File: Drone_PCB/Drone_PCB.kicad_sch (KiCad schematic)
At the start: 56 parts, among them J1 Conn_01x04_Pin, J2 Conn_01x08_Socket, J3 Conn_01x05_Socket, J4 Conn_01x02_Socket, J5 Conn_01x02_Socket, J6 Conn_01x02_Socket, J6 USB_B_Micro, J7 Conn_01x02_Socket, J8 Conn_01x02_Socket, Q1 BSS214NW, Q2 BSS214NW, Q3 AO3400A, Q4 AO3400A, Q5 AO3400A, Q6 AO3400A, SW2 SW_DPST_x2, U1 STM32F411RCT6, U2 AP2112K-3.3, U3 TP4056-42-ESOP8, U4 DW01A, Y1 26MHz

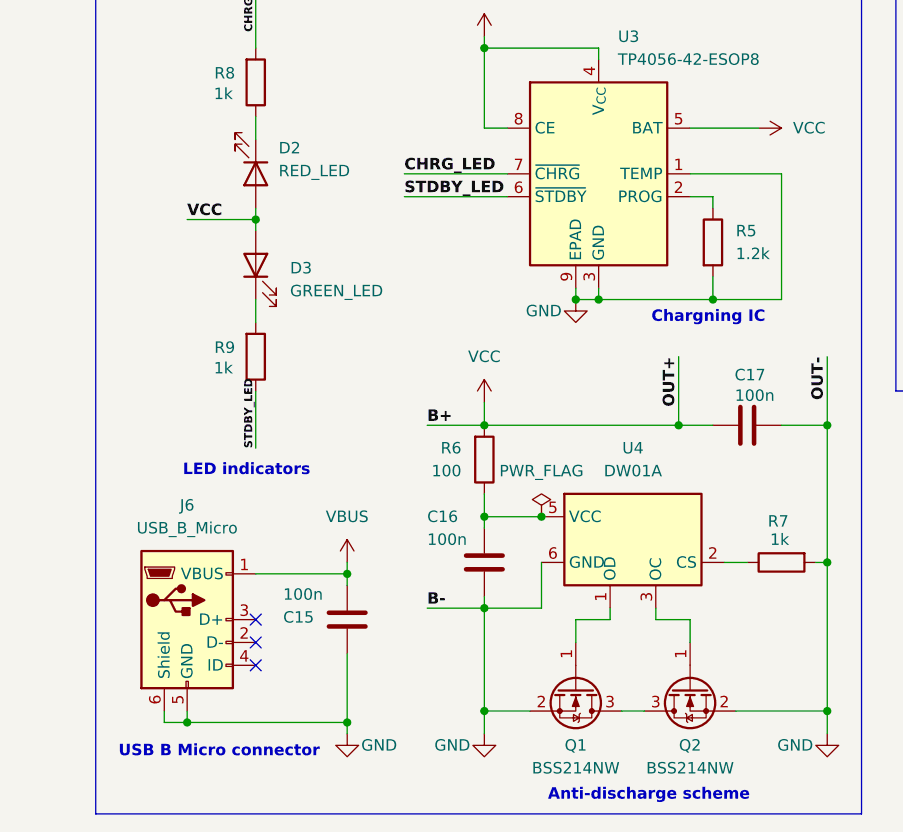
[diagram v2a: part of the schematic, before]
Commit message: Updated charging section
Changed NMOS transistors + diodes to VBUS
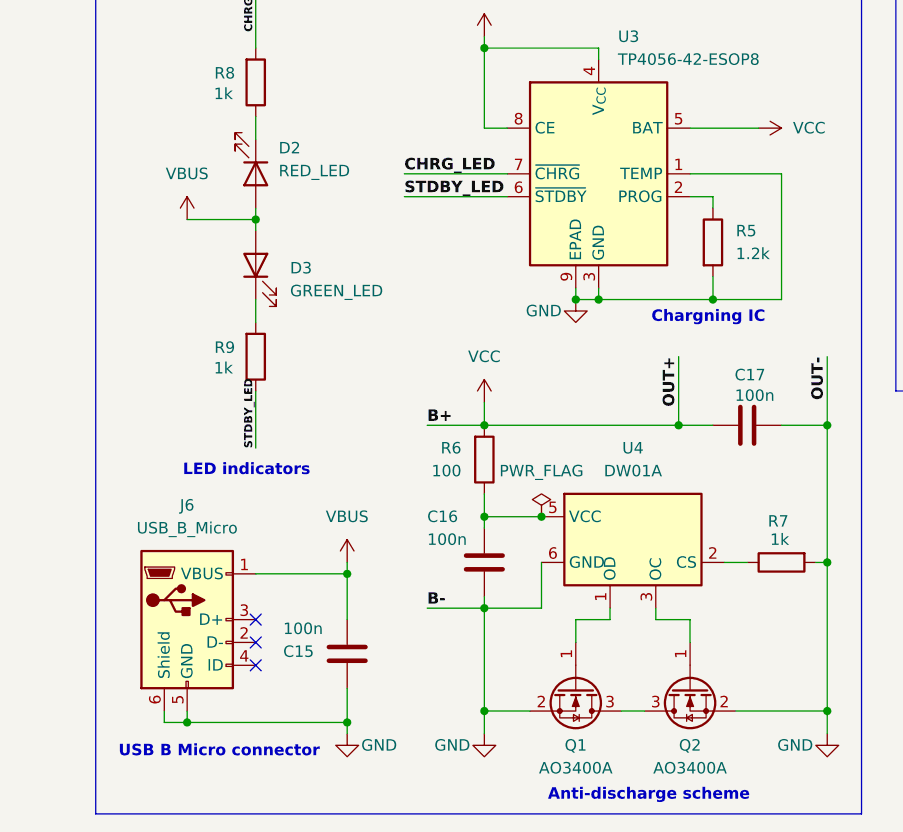
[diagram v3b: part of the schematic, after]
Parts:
- removed Q1, Q2: BSS214NW, Package_TO_SOT_SMD:SOT-323_SC-70, symbol Transistor_FET:BSS214NW
- added Q1, Q2: AO3400A, Package_TO_SOT_SMD:SOT-23, symbol Transistor_FET:AO3400A
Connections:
- net +3.3V: no longer D2.2 (A), D3.2 (A)
- net GND: now also Q1.2 (S), Q2.2 (S)
- net VBUS: now also D2.2 (A), D3.2 (A)
- net at U4.1 (OD): now also Q1.1 (G)
- net at U4.3 (OC): now also Q2.1 (G)
- new net: Q1.3 (D), Q2.3 (D)
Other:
- moved on the sheet: C15
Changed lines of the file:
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@@
 	)
 	(junction
+		(at 45.72 185.42)
+		(diameter 0)
+		(color 0 0 0 0)
+	)
+	(junction
 		(at 231.14 54.61)
 		(diameter 0)
@@
 	)
 	(junction
-		(at 45.72 185.42)
-		(diameter 0)
-		(color 0 0 0 0)
-	)
-	(junction
 		(at 220.98 132.08)
 		(diameter 0)
@@
 	(wire
 		(pts
+			(xy 45.72 181.61) (xy 45.72 185.42)
+		)
+		(stroke
+			(width 0)
+			(type default)
+		)
+	)
+	(wire
+		(pts
 			(xy 124.46 41.91) (xy 124.46 40.64)
 		)
@@
 	(wire
 		(pts
-			(xy 45.72 177.8) (xy 45.72 185.42)
-		)
-		(stroke
-			(width 0)
-			(type default)
-		)
-	)
-	(wire
-		(pts
 			(xy 43.18 45.72) (xy 48.26 45.72)
 		)
@@
 	(wire
 		(pts
-			(xy 45.72 168.91) (xy 45.72 170.18)
+			(xy 45.72 168.91) (xy 45.72 173.99)
 		)
 		(stroke
@@
 		)
 	)
-	(label "VCC"
-		(at 27.94 129.54 0)
-		(effects
-			(font
-				(size 1.27 1.27)
-				(thickness 0.254)
-				(bold yes)
-			)
-			(justify left bottom)
-		)
-	)
 	(label "UART_TX"
 		(at 156.21 88.9 0)
@@
 	)
 	(symbol
+		(lib_id "Transistor_FET:AO3400A")
+		(at 71.12 181.61 270)
+		(unit 1)
+		(exclude_from_sim no)
+		(in_bom yes)
+		(on_board yes)
+		(dnp no)
+		(fields_autoplaced yes)
+		(property "Reference" "Q1"
+			(at 71.12 187.96 90)
+			(effects
+				(font
+					(size 1.27 1.27)
+				)
+			)
+		)
+		(property "Value" "AO3400A"
+			(at 71.12 190.5 90)
+			(effects
+				(font
+					(size 1.27 1.27)
+				)
+			)
+		)
+		(property "Footprint" "Package_TO_SOT_SMD:SOT-23"
+			(at 69.215 186.69 0)
+			(effects
+				(font
+					(size 1.27 1.27)
+					(italic yes)
+				)
+				(justify left)
+				(hide yes)
+			)
+		)
+		(property "Datasheet" "http://www.aosmd.com/pdfs/datasheet/AO3400A.pdf"
+			(at 67.31 186.69 0)
+			(effects
+				(font
+					(size 1.27 1.27)
+				)
+				(justify left)
+				(hide yes)
+			)
+		)
+		(property "Description" "30V Vds, 5.7A Id, N-Channel MOSFET, SOT-23"
+			(at 71.12 181.61 0)
+			(effects
+				(font
+					(size 1.27 1.27)
+				)
+				(hide yes)
+			)
+		)
+		(pin "2"
+		)
+		(pin "3"
+		)
+		(pin "1"
+		)
+		(instances
+			(project "Drone_PCB"
+				(path "/2c198202-91eb-4035-8605-360d42f3c3f5"
+					(reference "Q1")
+					(unit 1)
+				)
+			)
+		)
+	)
+	(symbol
 		(lib_id "Switch:SW_DPST_x2")
 		(at 31.75 45.72 0)
@@
 	)
 	(symbol
-		(lib_id "Transistor_FET:BSS214NW")
-		(at 71.12 181.61 270)
-		(unit 1)
-		(exclude_from_sim no)
-		(in_bom yes)
-		(on_board yes)
-		(dnp no)
-		(fields_autoplaced yes)
-		(property "Reference" "Q1"
-			(at 71.12 187.96 90)
-			(effects
-				(font
-					(size 1.27 1.27)
-				)
-			)
-		)
-		(property "Value" "BSS214NW"
-			(at 71.12 190.5 90)
-			(effects
-				(font
-					(size 1.27 1.27)
-				)
-			)
-		)
-		(property "Footprint" "Package_TO_SOT_SMD:SOT-323_SC-70"
-			(at 69.215 186.69 0)
-			(effects
-				(font
-					(size 1.27 1.27)
-					(italic yes)
-				)
-				(justify left)
-				(hide yes)
-			)
-		)
-		(property "Datasheet" "https://www.infineon.com/dgdl/Infineon-BSS214NW-DS-v02_02-en.pdf?fileId=db3a30431b3e89eb011b695aebc01bde"
-			(at 67.31 186.69 0)
-			(effects
-				(font
-					(size 1.27 1.27)
-				)
-				(justify left)
-				(hide yes)
-			)
-		)
-		(property "Description" "20V Vds, 1.5A Id, N-Channel MOSFET, SOT-323"
-			(at 71.12 181.61 0)
-			(effects
-				(font
-					(size 1.27 1.27)
-				)
-				(hide yes)
-			)
-		)
-		(pin "1"
-		)
-		(pin "3"
-		)
-		(pin "2"
-		)
-		(instances
-			(project ""
-				(path "/2c198202-91eb-4035-8605-360d42f3c3f5"
-					(reference "Q1")
-					(unit 1)
-				)
-			)
-		)
-	)
-	(symbol
 		(lib_id "Device:R")
 		(at 93.98 167.64 90)
@@
 	(symbol
 		(lib_id "Device:C")
-		(at 45.72 173.99 0)
+		(at 45.72 177.8 0)
 		(mirror x)
 		(unit 1)
@@
 		(dnp no)
 		(property "Reference" "C15"
-			(at 38.608 173.736 0)
+			(at 38.608 177.546 0)
 			(effects
 				(font
@@
 		)
 		(property "Value" "100n"
-			(at 38.608 171.196 0)
+			(at 38.608 175.006 0)
 			(effects
 				(font
@@
 		)
 		(property "Footprint" "Capacitor_SMD:C_0402_1005Metric"
-			(at 46.6852 170.18 0)
+			(at 46.6852 173.99 0)
 			(effects
 				(font
@@
 		)
 		(property "Datasheet" "~"
-			(at 45.72 173.99 0)
+			(at 45.72 177.8 0)
 			(effects
 				(font
@@
 		)
 		(property "Description" "Unpolarized capacitor"
-			(at 45.72 173.99 0)
+			(at 45.72 177.8 0)
 			(effects
 				(font
@@
 	)
 	(symbol
+		(lib_id "power:VBUS")
+		(at 27.94 129.54 0)
+		(unit 1)
+		(exclude_from_sim no)
+		(in_bom yes)
+		(on_board yes)
+		(dnp no)
+		(fields_autoplaced yes)
+		(property "Reference" "#PWR033"
+			(at 27.94 133.35 0)
+			(effects
+				(font
+					(size 1.27 1.27)
+				)
+				(hide yes)
+			)
+		)
+		(property "Value" "VBUS"
+			(at 27.94 124.46 0)
+			(effects
+				(font
+					(size 1.27 1.27)
+				)
+			)
+		)
+		(property "Footprint" ""
+			(at 27.94 129.54 0)
+			(effects
+				(font
+					(size 1.27 1.27)
+				)
+				(hide yes)
+			)
+		)
+		(property "Datasheet" ""
+			(at 27.94 129.54 0)
+			(effects
+				(font
+					(size 1.27 1.27)
+				)
+				(hide yes)
+			)
+		)
+		(property "Description" "Power symbol creates a global label with name \"VBUS\""
+			(at 27.94 129.54 0)
+			(effects
+				(font
+					(size 1.27 1.27)
+				)
+				(hide yes)
+			)
+		)
+		(pin "1"
+		)
+		(instances
+			(project "Drone_PCB"
+				(path "/2c198202-91eb-4035-8605-360d42f3c3f5"
+					(reference "#PWR033")
+					(unit 1)
+				)
+			)
+		)
+	)
+	(symbol
 		(lib_id "Battery_Management:DW01A")
 		(at 77.47 165.1 0)
@@
 	)
 	(symbol
+		(lib_id "Transistor_FET:AO3400A")
+		(at 83.82 181.61 90)
+		(mirror x)
+		(unit 1)
+		(exclude_from_sim no)
+		(in_bom yes)
+		(on_board yes)
+		(dnp no)
+		(property "Reference" "Q2"
+			(at 83.82 187.96 90)
+			(effects
+				(font
+					(size 1.27 1.27)
+				)
+			)
+		)
+		(property "Value" "AO3400A"
+			(at 83.82 190.5 90)
+			(effects
+				(font
+					(size 1.27 1.27)
+				)
+			)
+		)
+		(property "Footprint" "Package_TO_SOT_SMD:SOT-23"
+			(at 85.725 186.69 0)
+			(effects
+				(font
+					(size 1.27 1.27)
+					(italic yes)
+				)
+				(justify left)
+				(hide yes)
+			)
+		)
+		(property "Datasheet" "http://www.aosmd.com/pdfs/datasheet/AO3400A.pdf"
+			(at 87.63 186.69 0)
+			(effects
+				(font
+					(size 1.27 1.27)
+				)
+				(justify left)
+				(hide yes)
+			)
+		)
+		(property "Description" "30V Vds, 5.7A Id, N-Channel MOSFET, SOT-23"
+			(at 83.82 181.61 0)
+			(effects
+				(font
+					(size 1.27 1.27)
+				)
+				(hide yes)
+			)
+		)
+		(pin "2"
+		)
+		(pin "3"
+		)
+		(pin "1"
+		)
+		(instances
+			(project "Drone_PCB"
+				(path "/2c198202-91eb-4035-8605-360d42f3c3f5"
+					(reference "Q2")
+					(unit 1)
+				)
+			)
+		)
+	)
+	(symbol
 		(lib_id "power:+3.3V")
 		(at 228.6 142.24 180)
@@
 					(unit 1)
 				)
-			)
-		)
-	)
-	(symbol
-		(lib_id "Transistor_FET:BSS214NW")
-		(at 83.82 181.61 90)
-		(mirror x)
-		(unit 1)
-		(exclude_from_sim no)
-		(in_bom yes)
-		(on_board yes)
-		(dnp no)
-		(property "Reference" "Q2"
-			(at 83.82 187.96 90)
-			(effects
-				(font
-					(size 1.27 1.27)
-				)
-			)
-		)
-		(property "Value" "BSS214NW"
-			(at 83.82 190.5 90)
-			(effects
-				(font
-					(size 1.27 1.27)
-				)
-			)
-		)
-		(property "Footprint" "Package_TO_SOT_SMD:SOT-323_SC-70"
-			(at 85.725 186.69 0)
-			(effects
-				(font
-					(size 1.27 1.27)
-					(italic yes)
-				)
-				(justify left)
-				(hide yes)
-			)
-		)
-		(property "Datasheet" "https://www.infineon.com/dgdl/Infineon-BSS214NW-DS-v02_02-en.pdf?fileId=db3a30431b3e89eb011b695aebc01bde"
-			(at 87.63 186.69 0)
-			(effects
-				(font
-					(size 1.27 1.27)
-				)
-				(justify left)
-				(hide yes)
-			)
-		)
-		(property "Description" "20V Vds, 1.5A Id, N-Channel MOSFET, SOT-323"
-			(at 83.82 181.61 0)
-			(effects
-				(font
-					(size 1.27 1.27)
-				)
-				(hide yes)
-			)
-		)
-		(pin "1"
-		)
-		(pin "3"
-		)
-		(pin "2"
-		)
-		(instances
-			(project "Drone_PCB"
-				(path "/2c198202-91eb-4035-8605-360d42f3c3f5"
-					(reference "Q2")
-					(unit 1)
-				)

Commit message: Added NRST button
Following the advice of Dr. Puchalski, I added NRST button. Additionally, I tidied up the engine area more.
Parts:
- added SW1: SW_MEC_5G, symbol Switch:SW_MEC_5G
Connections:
- net GND: now also SW1.3 (B), SW1.4 (B)
- net NRST: now also SW1.1 (A), SW1.2 (A)
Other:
- moved on the sheet: D6, D7, J1, J4, J5, J6, J7, Q5, Q6

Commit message: Switching THD Signal LED to SMD
It will be better I guess
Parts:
- removed J8: Conn_01x02_Socket, symbol Connector:Conn_01x02_Socket
- added D8: YELLOW_LED, symbol Device:LED
- added R11: 220, Resistor_SMD:R_0402_1005Metric, symbol Device:R
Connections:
- net GND: now also D8.1 (K)
- net LED_SIGNAL: now also R11.2
- new net: D8.2 (A), R11.1
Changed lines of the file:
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@@
 	(wire
 		(pts
-			(xy 148.59 105.41) (xy 154.94 105.41)
-		)
-		(stroke
-			(width 0)
-			(type default)
-		)
-	)
-	(wire
-		(pts
 			(xy 232.41 40.64) (xy 232.41 43.18)
 		)
@@
 	(wire
 		(pts
-			(xy 154.94 107.95) (xy 148.59 107.95)
-		)
-		(stroke
-			(width 0)
-			(type default)
-		)
-	)
-	(wire
-		(pts
 			(xy 147.32 40.64) (xy 147.32 41.91)
 		)
@@
 	(wire
 		(pts
+			(xy 154.94 107.95) (xy 154.94 109.22)
+		)
+		(stroke
+			(width 0)
+			(type default)
+		)
+	)
+	(wire
+		(pts
 			(xy 49.53 48.26) (xy 48.26 48.26)
 		)
@@
 	(wire
 		(pts
-			(xy 154.94 96.52) (xy 154.94 105.41)
-		)
-		(stroke
-			(width 0)
-			(type default)
-		)
-	)
-	(wire
-		(pts
 			(xy 35.56 138.43) (xy 35.56 140.97)
 		)
@@
 	(wire
 		(pts
-			(xy 154.94 109.22) (xy 154.94 107.95)
-		)
-		(stroke
-			(width 0)
-			(type default)
-		)
-	)
-	(wire
-		(pts
 			(xy 158.75 40.64) (xy 158.75 41.91)
 		)
@@
 	(wire
 		(pts
+			(xy 154.94 96.52) (xy 154.94 100.33)
+		)
+		(stroke
+			(width 0)
+			(type default)
+		)
+	)
+	(wire
+		(pts
 			(xy 228.6 104.14) (xy 228.6 105.41)
 		)
@@
 	)
 	(symbol
+		(lib_id "Device:LED")
+		(at 154.94 113.03 90)
+		(unit 1)
+		(exclude_from_sim no)
+		(in_bom yes)
+		(on_board yes)
+		(dnp no)
+		(property "Reference" "D8"
+			(at 146.05 112.776 90)
+			(effects
+				(font
+					(size 1.27 1.27)
+				)
+				(justify right)
+			)
+		)
+		(property "Value" "YELLOW_LED"
+			(at 141.986 115.316 90)
+			(effects
+				(font
+					(size 1.27 1.27)
+				)
+				(justify right)
+			)
+		)
+		(property "Footprint" ""
+			(at 154.94 113.03 0)
+			(effects
+				(font
+					(size 1.27 1.27)
+				)
+				(hide yes)
+			)
+		)
+		(property "Datasheet" "~"
+			(at 154.94 113.03 0)
+			(effects
+				(font
+					(size 1.27 1.27)
+				)
+				(hide yes)
+			)
+		)
+		(property "Description" "Light emitting diode"
+			(at 154.94 113.03 0)
+			(effects
+				(font
+					(size 1.27 1.27)
+				)
+				(hide yes)
+			)
+		)
+		(property "Sim.Pins" "1=K 2=A"
+			(at 154.94 113.03 0)
+			(effects
+				(font
+					(size 1.27 1.27)
+				)
+				(hide yes)
+			)
+		)
+		(pin "2"
+		)
+		(pin "1"
+		)
+		(instances
+			(project ""
+				(path "/2c198202-91eb-4035-8605-360d42f3c3f5"
+					(reference "D8")
+					(unit 1)
+				)
+			)
+		)
+	)
+	(symbol
 		(lib_id "Device:C")
 		(at 113.03 36.83 0)
@@
 	)
 	(symbol
-		(lib_id "Connector:Conn_01x02_Socket")
-		(at 143.51 107.95 180)
-		(unit 1)
-		(exclude_from_sim no)
-		(in_bom yes)
-		(on_board yes)
-		(dnp no)
-		(property "Reference" "J8"
-			(at 140.208 107.696 0)
-			(effects
-				(font
-					(size 1.27 1.27)
-				)
-			)
-		)
-		(property "Value" "Conn_01x02_Socket"
-			(at 140.208 110.236 0)
-			(effects
-				(font
-					(size 1.27 1.27)
-				)
-			)
-		)
-		(property "Footprint" ""
-			(at 143.51 107.95 0)
-			(effects
-				(font
-					(size 1.27 1.27)
-				)
-				(hide yes)
-			)
-		)
-		(property "Datasheet" "~"
-			(at 143.51 107.95 0)
-			(effects
-				(font
-					(size 1.27 1.27)
-				)
-				(hide yes)
-			)
-		)
-		(property "Description" "Generic connector, single row, 01x02, script generated"
-			(at 143.51 107.95 0)
-			(effects
-				(font
-					(size 1.27 1.27)
-				)
-				(hide yes)
-			)
-		)
-		(pin "1"
-		)
-		(pin "2"
-		)
-		(instances
-			(project "Drone_PCB"
-				(path "/2c198202-91eb-4035-8605-360d42f3c3f5"
-					(reference "J8")
-					(unit 1)
-				)
-			)
-		)
-	)
-	(symbol
 		(lib_id "Device:C")
 		(at 45.72 177.8 0)
@@
 	)
 	(symbol
+		(lib_id "Device:R")
+		(at 154.94 104.14 180)
+		(unit 1)
+		(exclude_from_sim no)
+		(in_bom yes)
+		(on_board yes)
+		(dnp no)
+		(property "Reference" "R11"
+			(at 151.384 103.124 0)
+			(effects
+				(font
+					(size 1.27 1.27)
+				)
+			)
+		)
+		(property "Value" "220"
+			(at 151.384 105.41 0)
+			(effects
+				(font
+					(size 1.27 1.27)
+				)
+			)
+		)
+		(property "Footprint" "Resistor_SMD:R_0402_1005Metric"
+			(at 156.718 104.14 90)
+			(effects
+				(font
+					(size 1.27 1.27)
+				)
+				(hide yes)
+			)
+		)
+		(property "Datasheet" "~"
+			(at 154.94 104.14 0)
+			(effects
+				(font
+					(size 1.27 1.27)
+				)
+				(hide yes)
+			)
+		)
+		(property "Description" "Resistor"
+			(at 154.94 104.14 0)
+			(effects
+				(font
+					(size 1.27 1.27)
+				)
+				(hide yes)
+			)
+		)
+		(pin "1"
+		)
+		(pin "2"
+		)
+		(instances
+			(project "Drone_PCB"
+				(path "/2c198202-91eb-4035-8605-360d42f3c3f5"
+					(reference "R11")
+					(unit 1)
+				)
+			)
+		)
+	)
+	(symbol
 		(lib_id "Device:C")
 		(at 135.89 36.83 0)
@@
 	(symbol
 		(lib_id "power:GND")
-		(at 154.94 109.22 0)
+		(at 154.94 116.84 0)
 		(unit 1)
 		(exclude_from_sim no)
@@
 		(fields_autoplaced yes)
 		(property "Reference" "#PWR014"
-			(at 154.94 115.57 0)
+			(at 154.94 123.19 0)
 			(effects
 				(font
@@
 		)
 		(property "Value" "GND"
-			(at 154.94 114.3 0)
+			(at 154.94 121.92 0)
 			(effects
 				(font
@@
 		)
 		(property "Footprint" ""
-			(at 154.94 109.22 0)
+			(at 154.94 116.84 0)
 			(effects
 				(font
@@
 		)
 		(property "Datasheet" ""
-			(at 154.94 109.22 0)
+			(at 154.94 116.84 0)
 			(effects
 				(font
@@
 		)
 		(property "Description" "Power symbol creates a global label with name \"GND\" , ground"
-			(at 154.94 109.22 0)
+			(at 154.94 116.84 0)
 			(effects
 				(font

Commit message: Changed TP4056 symbol
BAT is passive now due to KiCad errors about multiple Power Outputs
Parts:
- renumbered J6 to J8
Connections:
- net I2C_SCL renamed SCL
- net I2C_SDA renamed SDA
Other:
- note added: "I2C SCL"
- note added: "I2C SDA"
- note added: "UART RX"
- note added: "UART TX"
